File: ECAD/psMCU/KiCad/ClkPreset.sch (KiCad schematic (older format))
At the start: 6 parts

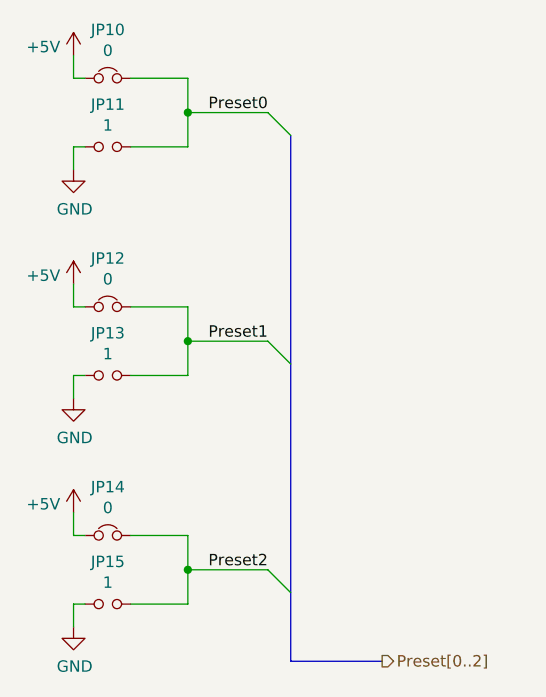
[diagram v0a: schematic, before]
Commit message: First draft v1.0 schematic done, ready for verify
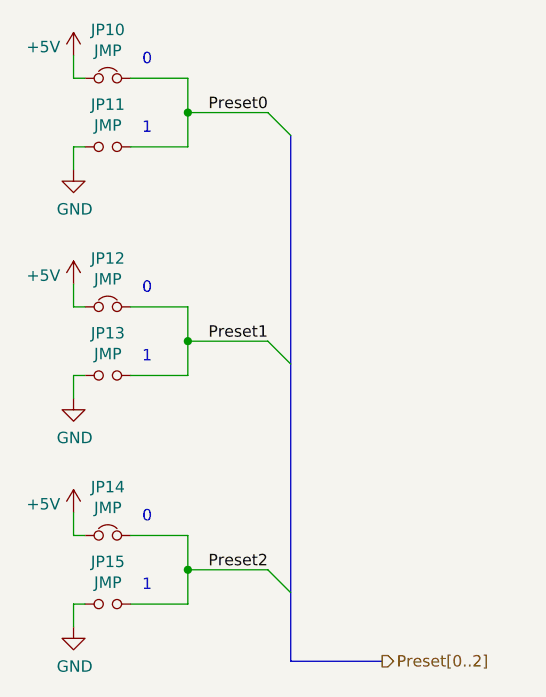
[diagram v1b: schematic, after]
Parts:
- JP10, JP12, JP14: value 0 -> JMP
- JP11, JP13, JP15: value 1 -> JMP
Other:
- note added: "0"
- note added: "1"
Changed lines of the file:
@@
 $Descr A4 11693 8268
 encoding utf-8
-Sheet 79 93
+Sheet 80 98
 Title "psMCU"
 Date "2021-03-30"
-Rev "v0.1"
+Rev "v1.0"
 Comp "Philipp Schilk"
 Comment1 ""
@@
 P 3850 1700
 F 0 "JP10" H 3850 1912 50  0000 C CNN
-F 1 "0" H 3850 1821 50  0000 C CNN
+F 1 "JMP" H 3850 1821 50  0000 C CNN
 F 2 "NoRef_Footprints:R_0603_1608Metric_NoRef" H 3850 1700 50  0001 C CNN
 F 3 "~" H 3850 1700 50  0001 C CNN
@@
 P 3850 2000
 F 0 "JP11" H 3850 2185 50  0000 C CNN
-F 1 "1" H 3850 2094 50  0000 C CNN
+F 1 "JMP" H 3850 2094 50  0000 C CNN
 F 2 "NoRef_Footprints:R_0603_1608Metric_NoRef" H 3850 2000 50  0001 C CNN
 F 3 "~" H 3850 2000 50  0001 C CNN
@@
 P 3850 2700
 F 0 "JP12" H 3850 2912 50  0000 C CNN
-F 1 "0" H 3850 2821 50  0000 C CNN
+F 1 "JMP" H 3850 2821 50  0000 C CNN
 F 2 "NoRef_Footprints:R_0603_1608Metric_NoRef" H 3850 2700 50  0001 C CNN
 F 3 "~" H 3850 2700 50  0001 C CNN
@@
 P 3850 3000
 F 0 "JP13" H 3850 3185 50  0000 C CNN
-F 1 "1" H 3850 3094 50  0000 C CNN
+F 1 "JMP" H 3850 3094 50  0000 C CNN
 F 2 "NoRef_Footprints:R_0603_1608Metric_NoRef" H 3850 3000 50  0001 C CNN
 F 3 "~" H 3850 3000 50  0001 C CNN
@@
 P 3850 3700
 F 0 "JP14" H 3850 3912 50  0000 C CNN
-F 1 "0" H 3850 3821 50  0000 C CNN
+F 1 "JMP" H 3850 3821 50  0000 C CNN
 F 2 "NoRef_Footprints:R_0603_1608Metric_NoRef" H 3850 3700 50  0001 C CNN
 F 3 "~" H 3850 3700 50  0001 C CNN
@@
 P 3850 4000
 F 0 "JP15" H 3850 4185 50  0000 C CNN
-F 1 "1" H 3850 4094 50  0000 C CNN
+F 1 "JMP" H 3850 4094 50  0000 C CNN
 F 2 "NoRef_Footprints:R_0603_1608Metric_NoRef" H 3850 4000 50  0001 C CNN
 F 3 "~" H 3850 4000 50  0001 C CNN
@@
 Wire Bus Line
 	4650 4250 5050 4250
+Text Notes 4000 1650 0    50   ~ 0
+0
+Text Notes 4000 1950 0    50   ~ 0
+1
+Text Notes 4000 2650 0    50   ~ 0
+0
+Text Notes 4000 3650 0    50   ~ 0
+0
+Text Notes 4000 2950 0    50   ~ 0
+1
+Text Notes 4000 3950 0    50   ~ 0
+1
 Wire Bus Line
 	4650 1950 4650 4250
